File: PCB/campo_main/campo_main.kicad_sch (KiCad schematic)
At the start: 13 parts, among them J1 MOTOR 1, J2 MOTOR 2, J3 GPIO, J4 MOTOR PWR, J5 I2C, J6 Raspberry_Pi_4, U2 CAT24C256

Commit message: Update schematic
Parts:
- removed C1: 100n, symbol Device:C_Small
- removed J6: Raspberry_Pi_4, Connector_PinSocket_2.54mm:PinSocket_2x20_P2.54mm_Vertical, symbol Connector:Raspberry_Pi_4
- removed JP1: ID_WP, symbol Jumper:SolderJumper_2_Open
- removed R1, R2: 3.9k, symbol Device:R_Small
- removed U2: CAT24C256, symbol Memory_EEPROM:CAT24C256
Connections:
- net +3V3 is gone; now on net +3.3V: J3.1 (Pin_1), J3.17 (Pin_17)
- net CSn is gone; now on net GPIO8/SPI0.CE0: A1.27 (GPIO21)
- net MISO is gone; now on net GPIO9/SPI0.MISO: A1.25 (GPIO19)
- net MOSI is gone; now on net GPIO10/SPI0.MOSI: A1.26 (GPIO20)
- net SCK is gone; now on net GPIO11/SPI0.SCLK: A1.29 (GPIO22)
- no-connect marks 7 -> 4
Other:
- note removed: "ID_SD and ID_SC PINS: These pins are reserved for HAT ID EEPROM. At boot time this I2C interface will be interrogated to look for an EEPROM that identifes the attached board and allows automagic setup of the GPIOs (and optionally, Linux drivers). Bridging JP1 enables write protection. DO NOT USE these pins for anything other than attaching an I2C ID EEPROM. Leave unconnected if ID EEPROM not requ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"
- moved on the sheet: A1, J1, J2, J4, J5, U1

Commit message: PCB update
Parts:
- added J6: UART, Connector_PinSocket_2.54mm:PinSocket_1x04_P2.54mm_Vertical, symbol Connector:Conn_01x04_Pin
- added J7: I2C, Connector_PinSocket_2.54mm:PinSocket_1x04_P2.54mm_Vertical, symbol Connector:Conn_01x04_Pin
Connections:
- net +3.3V: now also J1.4 (Pin_4), J2.4 (Pin_4), J5.2 (Pin_2), J6.4 (Pin_4), J7.2 (Pin_2); no longer J1.3 (Pin_3), J2.3 (Pin_3), J3.1 (Pin_1), J3.17 (Pin_17), J5.4 (Pin_4)
- net EN1A: now also A1.4 (GPIO2), J1.3 (Pin_3); no longer A1.15 (GPIO11), J1.4 (Pin_4)
- net EN1B: now also A1.5 (GPIO3), J1.2 (Pin_2); no longer A1.17 (GPIO13), J1.5 (Pin_5)
- net EN2A: now also A1.17 (GPIO13), J2.3 (Pin_3); no longer A1.22 (GPIO17), J2.4 (Pin_4)
- net EN2B: now also A1.19 (GPIO14), J2.2 (Pin_2); no longer A1.20 (GPIO15), J2.5 (Pin_5)
- net GND: now also A1.33 (AGND), J1.1 (Pin_1), J2.1 (Pin_1), J6.2 (Pin_2), J7.1 (Pin_1); no longer J1.6 (Pin_6), J2.6 (Pin_6)
- net GPIO10/SPI0.MOSI: now also A1.21 (GPIO16); no longer A1.26 (GPIO20)
- net GPIO11/SPI0.SCLK: now also A1.24 (GPIO18); no longer A1.29 (GPIO22)
- net GPIO14/TXD0: now also A1.1 (GPIO0), J6.1 (Pin_1)
- net GPIO15/RXD0: now also A1.2 (GPIO1), J6.3 (Pin_3)
- net GPIO2/SDA1: now also J7.4 (Pin_4)
- net GPIO3/SCL1: now also J7.3 (Pin_3)
- net GPIO8/SPI0.CE0: now also A1.22 (GPIO17); no longer A1.27 (GPIO21)
- net M1: now also J1.6 (Pin_6); no longer J1.1 (Pin_1)
- net M2: now also J1.5 (Pin_5); no longer J1.2 (Pin_2)
- net M3: now also J2.6 (Pin_6); no longer J2.1 (Pin_1)
- net M4: now also J2.5 (Pin_5); no longer J2.2 (Pin_2)
- net SCL: now also A1.7 (GPIO5); no longer A1.2 (GPIO1)
- net SDA: now also A1.6 (GPIO4), J5.4 (Pin_4); no longer A1.1 (GPIO0), J5.2 (Pin_2)
- net EEP: now reaches U1.1 (EEP)
- net EEP: now also A1.14 (GPIO10); no longer A1.5 (GPIO3)
- net IN3: now reaches U1.11 (IN3)
- net IN3: now also A1.10 (GPIO7); no longer A1.9 (GPIO6)
- net IN4: now reaches U1.12 (IN4)
- net IN4: now also A1.9 (GPIO6); no longer A1.10 (GPIO7)
- net IN2: now reaches A1.11 (GPIO8)
- net IN2: now also U1.8 (IN2); no longer U1.6 (ULT)
- net IN1: now reaches U1.7 (IN1)
- net IN1: now also A1.12 (GPIO9); no longer A1.6 (GPIO4)
- net G6: now reaches A1.16 (GPIO12)
- new net G15: A1.20 (GPIO15)
- new net ULT: A1.15 (GPIO11), U1.6 (ULT)
- no-connect marks 4 -> 3
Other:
- moved on the sheet: A1, J1, J2, J4, J5, U1

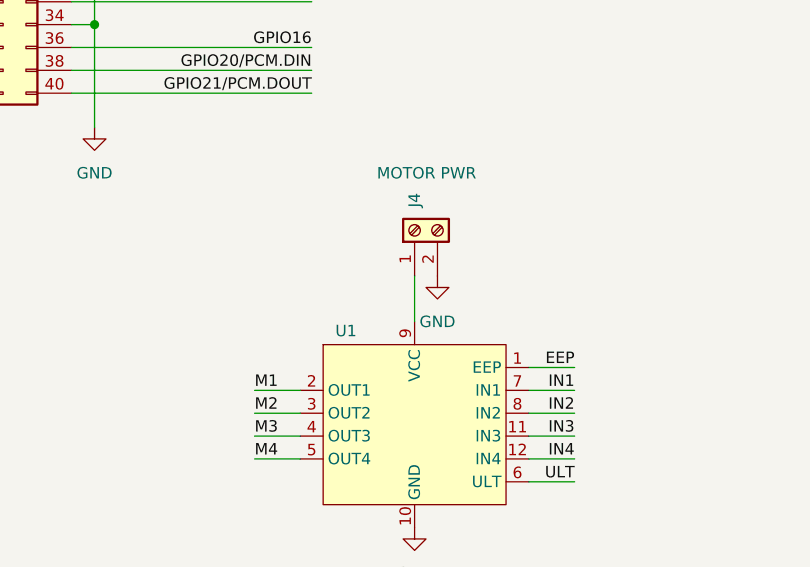
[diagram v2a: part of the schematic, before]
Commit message: Upgrade silkscreen
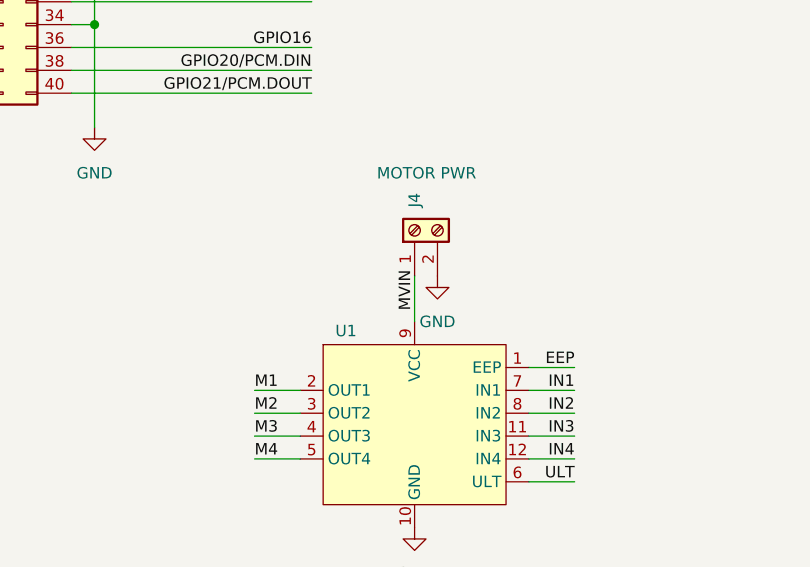
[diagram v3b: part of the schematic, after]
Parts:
- J5, J6, J7: footprint Connector_PinSocket_2.54mm:PinSocket_1x04_P2.54mm_Vertical -> Connector_PinHeader_2.54mm:PinHeader_1x04_P2.54mm_Vertical
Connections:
- net MVIN: now reaches J4.1 (Pin_1), U1.9 (VCC)
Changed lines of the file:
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@@
+		)
+	)
+	(label "MVIN"
+		(at 111.76 100.33 90)
+		(effects
+			(font
+				(size 1.27 1.27)
+			)
+			(justify left bottom)
 		)
 	)
@@
 			)
 		)
-		(property "Footprint" "Connector_PinSocket_2.54mm:PinSocket_1x04_P2.54mm_Vertical"
+		(property "Footprint" "Connector_PinHeader_2.54mm:PinHeader_1x04_P2.54mm_Vertical"
 			(at 158.75 158.75 0)
 			(effects
@@
 			)
 		)
-		(property "Footprint" "Connector_PinSocket_2.54mm:PinSocket_1x04_P2.54mm_Vertical"
+		(property "Footprint" "Connector_PinHeader_2.54mm:PinHeader_1x04_P2.54mm_Vertical"
 			(at 121.92 158.75 0)
 			(effects
@@
 			)
 		)
-		(property "Footprint" "Connector_PinSocket_2.54mm:PinSocket_1x04_P2.54mm_Vertical"
+		(property "Footprint" "Connector_PinHeader_2.54mm:PinHeader_1x04_P2.54mm_Vertical"
 			(at 86.36 158.75 0)
 			(effects

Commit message: Fix for PCB
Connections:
- net GND: now also J4.1 (Pin_1); no longer J4.2 (Pin_2)
- net GPIO14/TXD0: now also A1.27 (GPIO21); no longer A1.1 (GPIO0), J6.1 (Pin_1)
- net GPIO15/RXD0: now also A1.26 (GPIO20); no longer A1.2 (GPIO1), J6.3 (Pin_3)
- net MVIN: now also J4.2 (Pin_2); no longer J4.1 (Pin_1)
- net G15: no longer names the net of A1.20 (GPIO15)
- net G6: no longer names the net of A1.16 (GPIO12)
- new net RX: A1.2 (GPIO1), J6.3 (Pin_3)
- new net TX: A1.1 (GPIO0), J6.1 (Pin_1)
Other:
- moved on the sheet: J4
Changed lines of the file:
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@@
+	(wire
+		(pts
+			(xy 73.66 35.56) (xy 100.33 35.56)
+		)
+		(stroke
+			(width 0)
+			(type default)
+		)
+	)
 	(wire
 		(pts
@@
 	(wire
 		(pts
-			(xy 73.66 35.56) (xy 105.41 35.56)
-		)
-		(stroke
-			(width 0)
-			(type solid)
-		)
-	)
-	(wire
-		(pts
 			(xy 58.42 38.1) (xy 58.42 58.42)
 		)
@@
 	(wire
 		(pts
-			(xy 163.83 113.03) (xy 167.64 113.03)
+			(xy 213.36 95.25) (xy 240.03 95.25)
 		)
 		(stroke
@@
 	(wire
 		(pts
-			(xy 163.83 120.65) (xy 167.64 120.65)
+			(xy 73.66 38.1) (xy 100.33 38.1)
 		)
 		(stroke
@@
 	(wire
 		(pts
-			(xy 73.66 38.1) (xy 105.41 38.1)
-		)
-		(stroke
-			(width 0)
-			(type solid)
-		)
-	)
-	(wire
-		(pts
 			(xy 213.36 90.17) (xy 231.14 90.17)
 		)
@@
 	(wire
 		(pts
+			(xy 213.36 97.79) (xy 240.03 97.79)
+		)
+		(stroke
+			(width 0)
+			(type default)
+		)
+	)
+	(wire
+		(pts
 			(xy 73.66 71.12) (xy 100.33 71.12)
 		)
@@
 			(width 0)
 			(type default)
-		)
-	)
-	(label "RX"
-		(at 105.41 38.1 180)
-		(effects
-			(font
-				(size 1.27 1.27)
-			)
-			(justify right bottom)
 		)
 	)
@@
 		)
 	)
-	(label "G15"
-		(at 163.83 120.65 0)
-		(effects
-			(font
-				(size 1.27 1.27)
-			)
-			(justify left bottom)
-		)
-	)
 	(label "M4"
 		(at 93.98 116.84 0)
@@
 		)
 	)
-	(label "TX"
-		(at 105.41 35.56 180)
-		(effects
-			(font
-				(size 1.27 1.27)
-			)
-			(justify right bottom)
-		)
-	)
 	(label "M3"
 		(at 93.98 114.3 0)
@@
 		)
 	)
-	(label "G6"
-		(at 163.83 113.03 0)
-		(effects
-			(font
-				(size 1.27 1.27)
-			)
-			(justify left bottom)
-		)
-	)
 	(label "GPIO19{slash}PCM.FS"
 		(at 31.75 71.12 0)
@@
 		)
 	)
+	(label "GPIO15{slash}RXD0"
+		(at 240.03 95.25 180)
+		(effects
+			(font
+				(size 1.27 1.27)
+			)
+			(justify right bottom)
+		)
+	)
 	(label "EN2A"
 		(at 54.61 161.29 180)
+		(effects
+			(font
+				(size 1.27 1.27)
+			)
+			(justify right bottom)
+		)
+	)
+	(label "GPIO14{slash}TXD0"
+		(at 240.03 97.79 180)
 		(effects
 			(font
@@
 	(symbol
 		(lib_id "Connector:Screw_Terminal_01x02")
-		(at 111.76 91.44 90)
+		(at 114.3 91.44 270)
+		(mirror x)
 		(unit 1)
 		(exclude_from_sim no)
@@
 		(dnp no)
 		(property "Reference" "J4"
-			(at 111.7599 88.9 0)
+			(at 114.3001 88.9 0)
 			(effects
 				(font
@@
 		)
 		(property "Value" "MOTOR PWR"
-			(at 118.618 85.09 90)
+			(at 107.442 85.09 90)
 			(effects
 				(font
@@
 		)
 		(property "Footprint" "TerminalBlock_4Ucon:TerminalBlock_4Ucon_1x02_P3.50mm_Horizontal"
-			(at 111.76 91.44 0)
+			(at 114.3 91.44 0)
 			(effects
 				(font
@@
 		)
 		(property "Datasheet" "~"
-			(at 111.76 91.44 0)
+			(at 114.3 91.44 0)
 			(effects
 				(font
@@
 		)
 		(property "Description" "Generic screw terminal, single row, 01x02, script generated (kicad-library-utils/schlib/autogen/connector/)"
-			(at 111.76 91.44 0)
-			(effects
-				(font
+			(at 114.3 91.44 0)
+			(effects
+				(font

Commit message: Some PCB Changes
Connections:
- no-connect marks 3 -> 10
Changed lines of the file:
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@@
+	)
+	(no_connect
+		(at 213.36 113.03)
+	)
+	(no_connect
+		(at 213.36 115.57)
+	)
+	(no_connect
+		(at 213.36 110.49)
 	)
 	(no_connect
@@
 	)
 	(no_connect
+		(at 167.64 113.03)
+	)
+	(no_connect
+		(at 167.64 120.65)
+	)
+	(no_connect
 		(at 167.64 77.47)
 	)
 	(no_connect
+		(at 190.5 59.69)
+	)
+	(no_connect
+		(at 213.36 100.33)
+	)
+	(no_connect
